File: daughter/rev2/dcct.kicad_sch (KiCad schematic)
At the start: 38 parts, among them U33 AD8429BRZ, U34 AD8675ARZ, U36 LTC6363IMS8, U37 LTC2376CDE-20

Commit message: Rename versions
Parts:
- removed C159: 0.01uF, Capacitor_SMD:C_0402_1005Metric, symbol Device:C_Small
- removed C161: 10uF, Capacitor_SMD:C_0603_1608Metric, symbol Device:C_Small
- removed C163: 0.1uF, Capacitor_SMD:C_0402_1005Metric, symbol Device:C_Small
- removed C167, C169: 6800pF, Capacitor_SMD:C_0402_1005Metric, symbol Device:C_Small
- removed C168: 3300pF, Capacitor_SMD:C_0402_1005Metric, symbol Device:C_Small
- removed R58: 1.3K, Resistor_SMD:R_0402_1005Metric, symbol Device:R_US
- removed R63: 15, Resistor_SMD:R_0402_1005Metric, symbol Device:R_US
- removed U34: AD8675ARZ, Package_SO:SOIC-8_3.9x4.9mm_P1.27mm, symbol PSC:AD8675ARZ
- removed U36: LTC6363IMS8, Package_SO:MSOP-8_3x3mm_P0.65mm, symbol PSC:LTC6363xMS8
- added C109: 3nF, Capacitor_SMD:C_0603_1608Metric, symbol Device:C_Small
- added C111: 2nF, Capacitor_SMD:C_0603_1608Metric, symbol Device:C_Small
- added C113, C150: 0.1uF, Capacitor_SMD:C_0402_1005Metric, symbol Device:C_Small
- added C114: 10uF, Capacitor_SMD:C_0603_1608Metric, symbol Device:C_Small
- added C120, C122: 470pF, Capacitor_SMD:C_0402_1005Metric, symbol Device:C_Small
- added D8: BAT54S, Package_TO_SOT_SMD:SOT-23, symbol Diode:BAT54S
- added R37, R39, R40, R45, R47, R51, R77: 10.0K, Resistor_SMD:R_0603_1608Metric, symbol Device:R_US
- added U21: THP210DR, myparts:SOIC_210DR_TEX, symbol PSC:THP210DR
- added U4: AD8676xR, Package_SO:SOIC-8_3.9x4.9mm_P1.27mm, symbol Amplifier_Operational:AD8676xR
- R62: value 10 -> 10.0K; footprint Resistor_SMD:R_0402_1005Metric -> Resistor_SMD:R_0603_1608Metric; MFG Panasonic -> Yageo; MFG_PN ERJ-2RKF10R0X -> RT0603BRB0710KL; PPM (none) -> 10ppm/C
- U37: footprint DFN-16_DE_LIT -> myparts:DFN-16_DE_LIT
- renumbered C171 to C136, C173 to C137, C175 to C138, C172 to C139, C174 to C149
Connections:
- net +15V: no longer C162.1, C165.1
- net +5.3VA: now also C162.1, C165.1, D8.2 (K), U21.3 (VS+), U21.7 (PD*), U4.8 (V+)
- net -5.3VA: now also C113.1, C114.1, D8.1 (A), U21.6 (VS-), U4.4 (V-)
- net GND: now also C113.2, C114.2, C150.2, R51.2, U4.3 (+), U4.5 (+)
- net drv_vref: now also C150.1, U21.2 (VOCM)
- net at R65.2: now also R62.1, C122.1, U21.4 (OUT+)
- net at R64.2: now also C120.2, R47.1, U21.5 (OUT-)
- net at R62.2: now also C122.2, R51.1, U21.1 (IN-)
- net at U33.7: now also D8.3 (COM), R77.2
- new net: C111.1, R39.1, R40.2, U4.6 (-)
- new net: C111.2, R40.1, R45.2, U4.7
- new net: C120.1, R45.1, R47.2, U21.8 (IN+)
- new net: C109.1, R37.2, R77.1, U4.2 (-)
- new net: C109.2, R37.1, R39.2, U4.1
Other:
- note removed: "Replace with ADA4945-1"
- moved on the sheet: C136, C137, C138, C139, C149, C151, C152, C154, C156, C158, C162, C165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

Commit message: Rework schematic with separate volt_ref block
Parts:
- added C161: 10uF, Capacitor_SMD:C_0603_1608Metric, symbol Device:C_Small
- added C175: 0.1uF, Capacitor_SMD:C_0402_1005Metric, symbol Device:C_Small
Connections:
- net GND: now also C161.2, C175.2
- net adc_vref: now also C161.1, C175.1

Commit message: Update BOM
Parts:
- C109: Cost (none) -> .14; MFG Kemet -> Murata; MFG_PN C0603C302J3GACTU -> C0603C302J5GACTU
- C111: Cost (none) -> .90
- C113, C137, C149, C150, C152, C158, C165, C175, C179, C181: Cost (none) -> .01
- C114, C136, C139, C154, C156, C161, C162, C178, C180: Cost (none) -> .07
- C138, C177: Cost (none) -> .01; MFG_PN CAP CER 3300PF 50V X7R 0402 -> CL05B682KB5NNNC
- D8: Cost (none) -> .1; MFG (none) -> Diotec Semiconductor; MFG_PN (none) -> BAT54S
- U21: Cost (none) -> 3.46; MFG (none) -> TI; MFG_PN (none) -> THP210DR
- U4: Cost (none) -> 5.91; MFG (none) -> Analog Devices; MFG_PN (none) -> AD8676BRZ

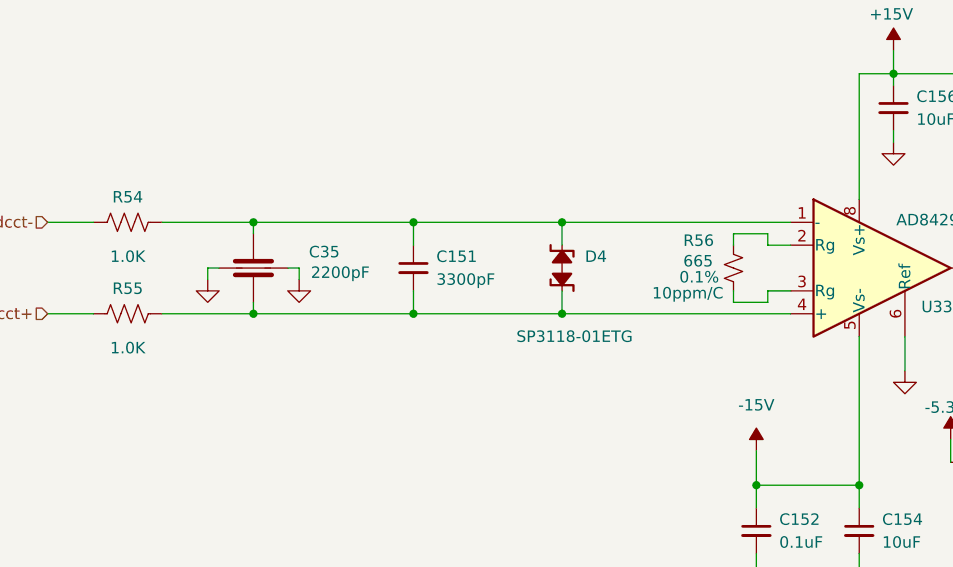
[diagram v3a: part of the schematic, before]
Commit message: Add parallel resistor for AD8429 gain to be exactly 10
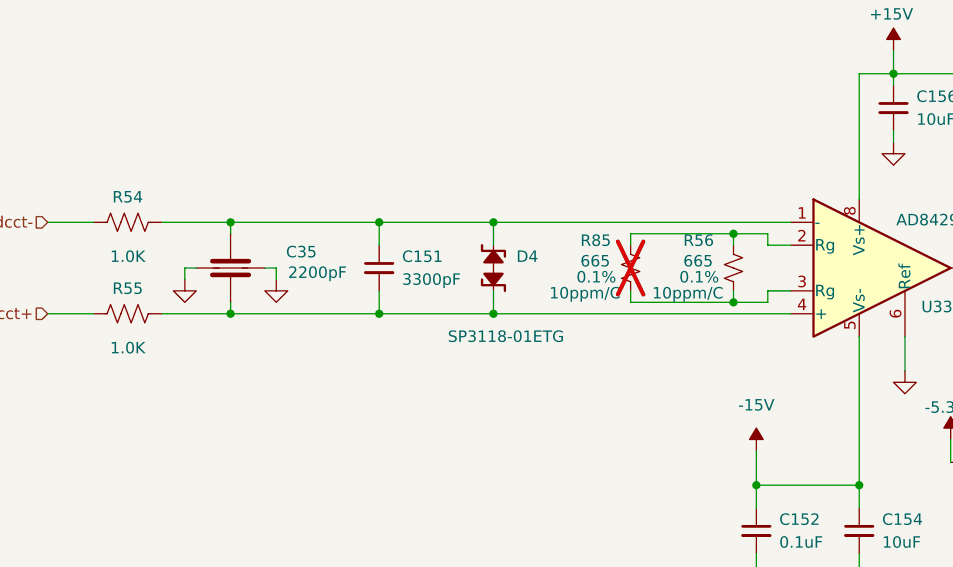
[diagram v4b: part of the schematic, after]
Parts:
- added R85: 665, Resistor_SMD:R_0603_1608Metric, symbol Device:R_Small_US
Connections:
- net at R56.1, U33.2 (Rg): now also R85.1
- net at R56.2, U33.3 (Rg): now also R85.2
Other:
- moved on the sheet: C151, C35, D4
